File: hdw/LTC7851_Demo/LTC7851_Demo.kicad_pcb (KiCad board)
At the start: 4 copper layers, 220 parts, among them J1101 FG_LOAD, J1102 ISNS, J1103 ISNS, J1201 ISNS, J1202 ISNS, J1301 ISNS, J1302 ISNS, J1401 VOUT, J1402 LOOP_TAP, J1403 Wave_Gen_In, J201 +12VIN, J202 +12VIN, J203 +12VIN, J204 GNDIN, J205 GNDIN, J206 GNDIN, J301 CLKOUT, J302 RUN, J303 SMOD, J304 IAVG, J901 +5V OUT, J902 +5V OUT, J903 GND OUT, J904 GND OUT, Q1101 BSC123N10LSGATMA1, Q1102 BSC123N10LSGATMA1, Q1201 BSC123N10LSGATMA1, Q1202 BSC123N10LSGATMA1, Q1301 BSC123N10LSGATMA1, Q1302 BSC123N10LSGATMA1, Q201 BSC123N10LSGATMA1, Q202 BSC123N10LSGATMA1, T1401 1:1 Pulse Transformer, U1101 LT1010DD, U201 LTC4365DDB, U202 74LVC1G06, U301 LTC7851UHH, U302 74LVC1G17, U303 74LVC1G06, U304 74LVC1G06, U401 SiC779, U501 SiC779, U601 SiC779, U701 SiC779, U801 LM1117-ADJ

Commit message: Board outline, mounting holes placed
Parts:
- C1103: moved to B.Cu
- moved MH1001 240.1 mm to (3.00, -47.0)
- moved MH1003 229.4 mm to (97.0, -47.0)
- moved MH1002 223.2 mm to (50.0, -47.0)
- moved MH1004 190.3 mm to (3.00, -3.00)
- moved MH1005 184.6 mm to (50.0, -3.00)
- moved MH1006 180.3 mm to (97.0, -3.00)
- moved J1302 140.4 mm to (166.9, 177.4), turned to 270 degrees
- moved R1103 138.5 mm to (168.1, 134.8), turned to 180 degrees
- moved J1301 138.4 mm to (166.9, 164.7), turned to 270 degrees
- moved R1106 138.3 mm to (168.1, 120.5), turned to 180 degrees
- moved J1103 138.2 mm to (166.9, 113.9), turned to 270 degrees
- moved R1104 137.6 mm to (168.1, 122.1), turned to 180 degrees
- moved R1306 131.7 mm to (165.7, 181.2), turned to 180 degrees
- moved J1202 131.3 mm to (166.9, 152.0), turned to 270 degrees
- moved R1105 129.9 mm to (168.1, 133.2), turned to 180 degrees
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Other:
- board outline added: 100 x 50 mm
- board text added: "Active Load"
- board text added: "Load Gate Driver"

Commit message: Arranged components for phase 1
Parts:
- moved C401 200.5 mm to (235.0, 94.4)
- moved C403 200.5 mm to (235.0, 93.1)
- moved C404 200.5 mm to (250.2, 83.2)
- moved C406 200.5 mm to (250.1, 85.4)
- moved R402 200.5 mm to (244.2, 92.3)
- moved R404 200.5 mm to (250.0, 86.8)
- moved R409 200.5 mm to (243.4, 93.7)
- moved R410 200.5 mm to (250.0, 88.3)
- moved C402 200.5 mm to (237.8, 92.9)
- moved R401 200.5 mm to (247.1, 89.4)
- moved R403 200.5 mm to (252.9, 83.3)
- moved R408 200.5 mm to (252.8, 86.2)
- moved R411 200.5 mm to (246.8, 92.4)
- moved C408 82.4 mm to (-32.4, 42.3)
- moved C418 77.3 mm to (-24.8, 68.1), turned to 270 degrees
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
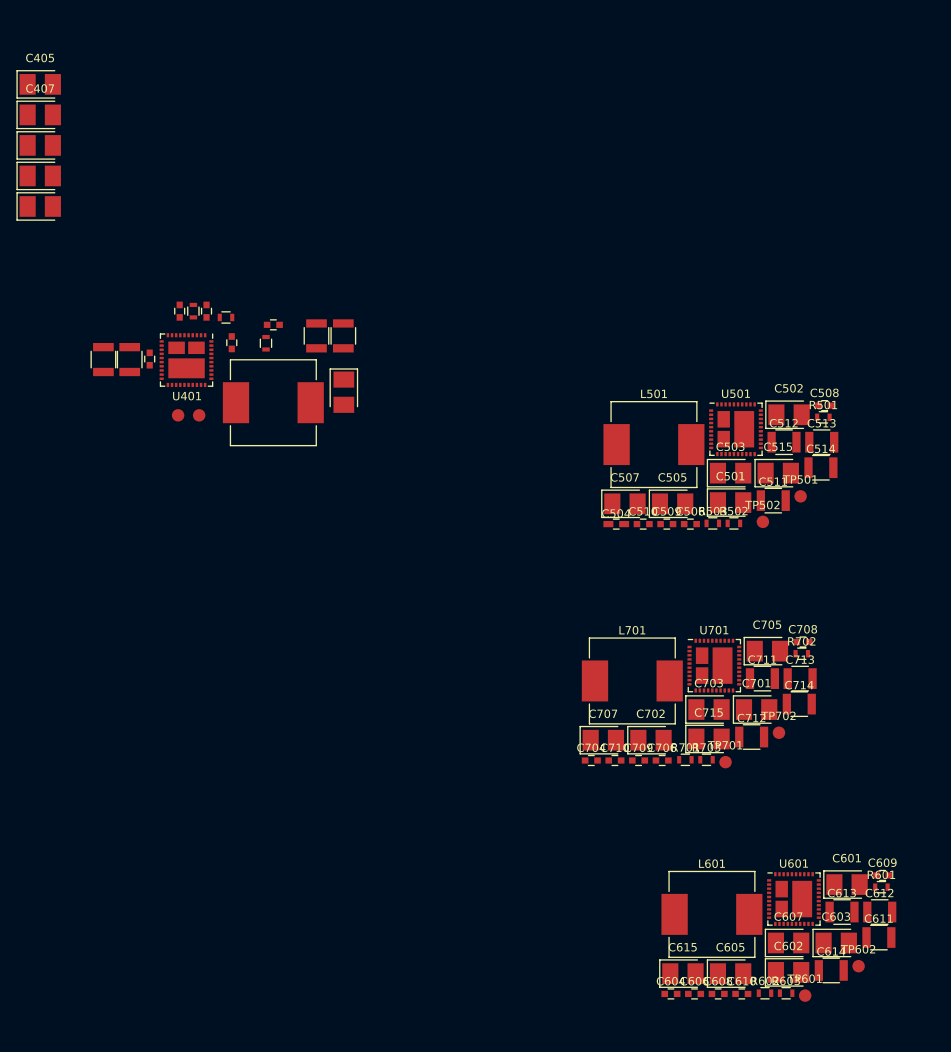
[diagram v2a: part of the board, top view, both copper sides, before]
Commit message: Duplicated phase 1 four times and changed ref des
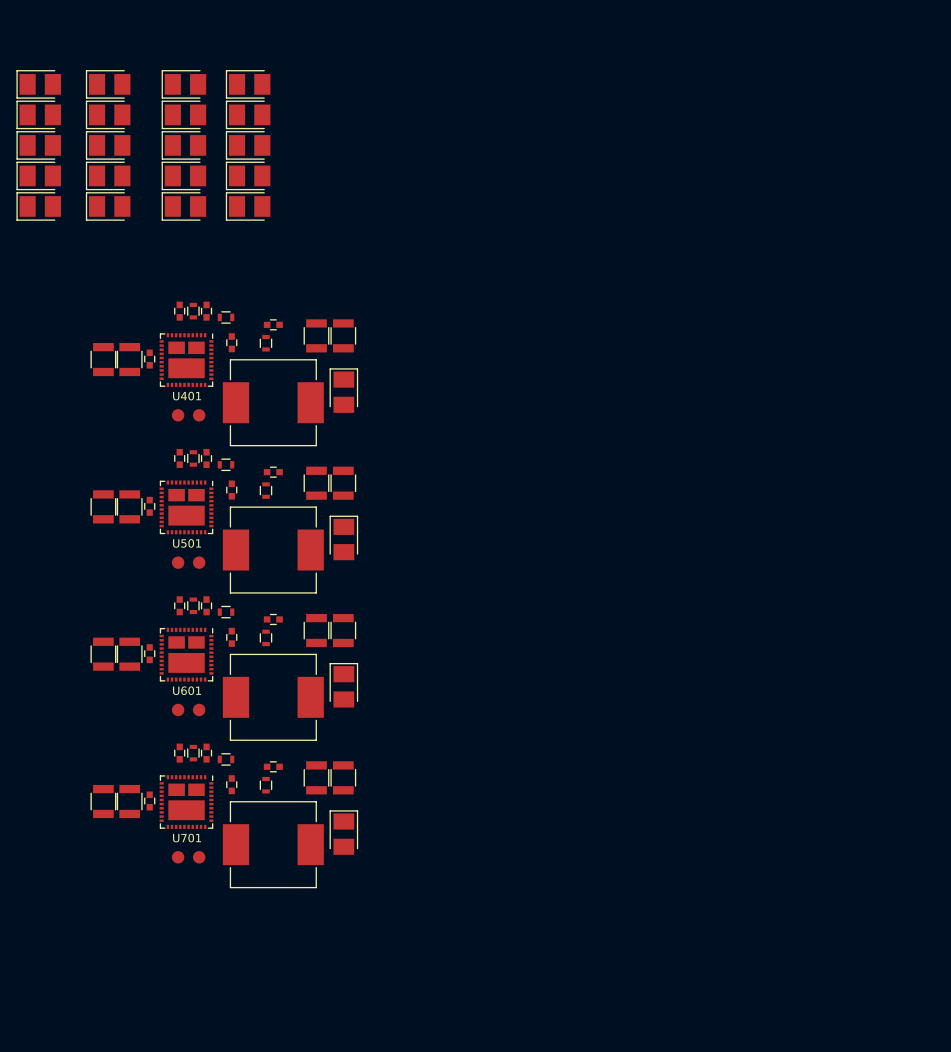
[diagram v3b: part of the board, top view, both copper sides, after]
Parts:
- C504: footprint Capacitors_SMD:C_0603_HandSoldering -> Capacitors_SMD:C_0603
- moved C602 126.5 mm to (-14.9, 38.6)
- moved C601 125.3 mm to (-14.9, 34.9)
- moved C603 124.2 mm to (-14.9, 42.3)
- moved C605 116.6 mm to (-14.9, 46.0)
- moved C607 114.9 mm to (-14.9, 49.7)
- moved C701 97.1 mm to (-7.11, 34.9)
- moved C611 96.7 mm to (-21.6, 103.7), turned to 270 degrees
- moved C613 94.4 mm to (-24.8, 103.7), turned to 270 degrees
- moved C609 92.4 mm to (-19.2, 103.6), turned to 270 degrees
- moved C501 90.3 mm to (-24.0, 34.9)
- moved C702 89.7 mm to (-7.11, 38.6)
- moved C502 89.6 mm to (-24.0, 38.6)
- moved C703 87.8 mm to (-7.11, 42.3)
- moved C513 87.0 mm to (-24.8, 85.9), turned to 270 degrees
- moved R601 85.8 mm to (-9.97, 98.6)
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
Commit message: Placed phases on board
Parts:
- removed J1103, J1201, J1202, J1301, J1302: ISNS, Pin_Headers:Pin_Header_Straight_1x02_Pitch2.54mm
- J1102, Q1101, Q1102, Q1201, Q1202, Q1301, Q1302, R1103, R1104, R1105, R1106, R1107, R1108, R1201, R1202, R1203, R1204, R1205, R1206, R1301, R1302, R1303, R1304, R1305, R1306: moved to B.Cu
- moved J904 202.2 mm to (23.4, -4.95)
- moved J901 198.8 mm to (40.3, -4.95)
- moved J903 183.0 mm to (66.0, -4.95)
- moved J902 178.2 mm to (82.9, -4.95)
- moved C713 175.4 mm to (40.2, -41.4), turned to 180 degrees
- moved C711 171.2 mm to (40.2, -38.2), turned to 180 degrees
- moved C709 168.1 mm to (40.3, -35.8), turned to 180 degrees
- moved TP701 168.0 mm to (33.5, -32.4), turned to 270 degrees
- moved C613 166.8 mm to (57.5, -41.4), turned to 180 degrees
- moved TP702 164.8 mm to (33.5, -29.8), turned to 270 degrees
- moved C611 162.5 mm to (57.5, -38.2), turned to 180 degrees
- moved U701 162.5 mm to (40.1, -31.4), turned to 180 degrees
- moved C513 161.6 mm to (74.7, -41.4), turned to 180 degrees
- moved C708 160.1 mm to (46.0, -32.2), turned to 180 degrees
- moved C418 160.1 mm to (92.0, -41.4), turned to 180 degrees
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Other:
- board text added: "-VOUT+"

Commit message: Finished arranging parts on board
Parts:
- removed J202, J203: +12VIN, Custom Footprints Library:Keystone_8191
- removed J204, J205: GNDIN, Custom Footprints Library:Keystone_8191
- C1101, C1102, C302, C303, C405, C407, C408, C410, C412, C501, C502, C503, C505, C507, C601, C602, C603, C605, C701, R1101, R1102, R302, R310, U1101: moved to B.Cu
- J1102: moved to F.Cu
- J201: value +12VIN -> +12V IN; footprint Custom Footprints Library:Keystone_8191 -> Custom Footprints Library:Wuerth_7461096_M4_Shank_9pos
- J206: value GNDIN -> GND IN; footprint Custom Footprints Library:Keystone_8191 -> Custom Footprints Library:Wuerth_7461096_M4_Shank_9pos
- TP201: footprint Pin_Headers:Pin_Header_Angled_1x01_Pitch2.54mm -> Pin_Headers:Pin_Header_Straight_1x01_Pitch2.54mm
- moved C603 196.8 mm to (171.8, 104.6), turned to 90 degrees
- moved C601 192.3 mm to (164.4, 104.6), turned to 90 degrees
- moved C605 192.1 mm to (168.1, 104.6), turned to 90 degrees
- moved C701 189.7 mm to (166.4, 111.7), turned to 270 degrees
- moved C505 189.4 mm to (153.6, 111.6), turned to 270 degrees
- moved C507 189.2 mm to (157.1, 104.6), turned to 90 degrees
- moved C602 187.6 mm to (160.7, 104.6), turned to 90 degrees
- moved C503 187.2 mm to (149.9, 111.6), turned to 270 degrees
- moved C702 176.5 mm to (151.9, 115.1), turned to 180 degrees
- moved C502 176.3 mm to (136.6, 111.4), turned to 270 degrees
- moved C501 174.6 mm to (132.9, 111.4), turned to 270 degrees
- moved C412 164.1 mm to (122.3, 104.5), turned to 90 degrees
- moved J1403 163.7 mm to (90.3, 113.4), turned to 90 degrees
- moved C407 161.1 mm to (111.3, 111.5), turned to 270 degrees
- moved C405 159.6 mm to (107.7, 111.5), turned to 270 degrees
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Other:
- board text removed: "+5.5 MNG"
- board text removed: "Active Load"
- board text removed: "Load Gate Driver"

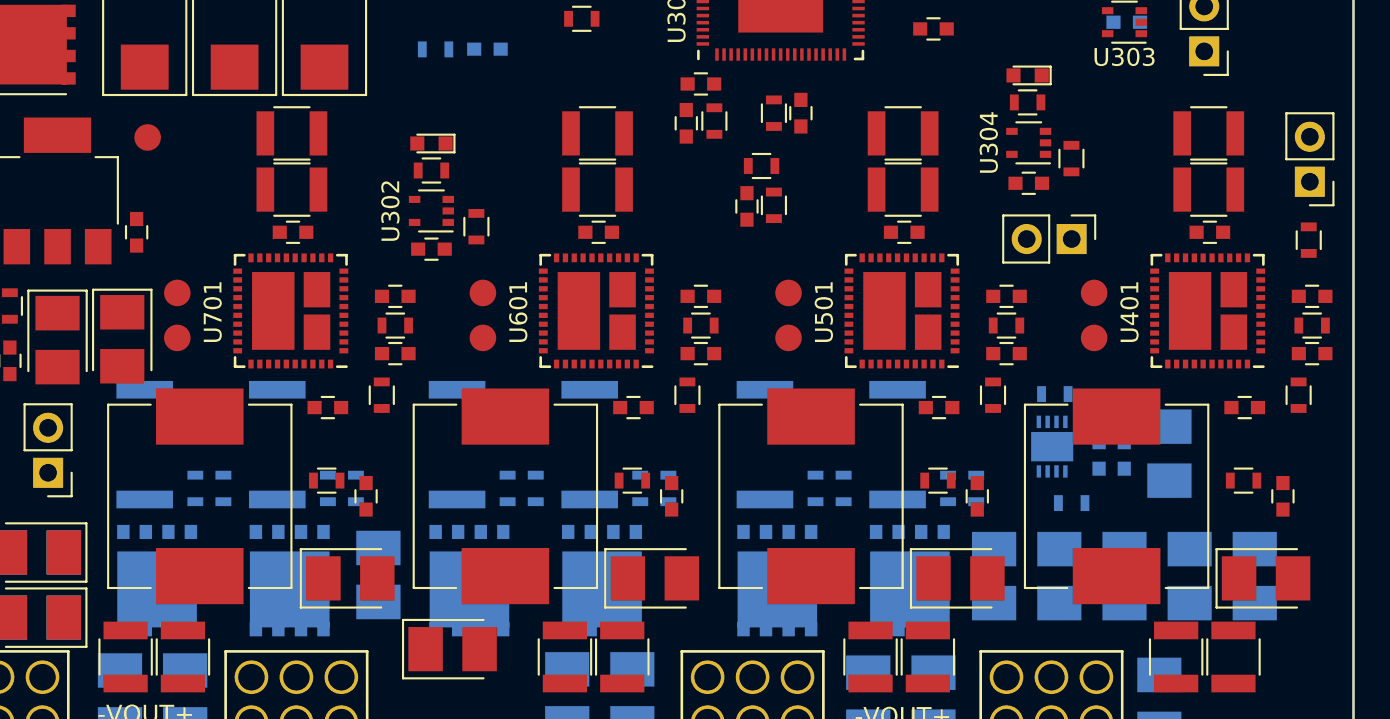
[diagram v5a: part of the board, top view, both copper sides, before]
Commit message: Flipped order of phases on PCB
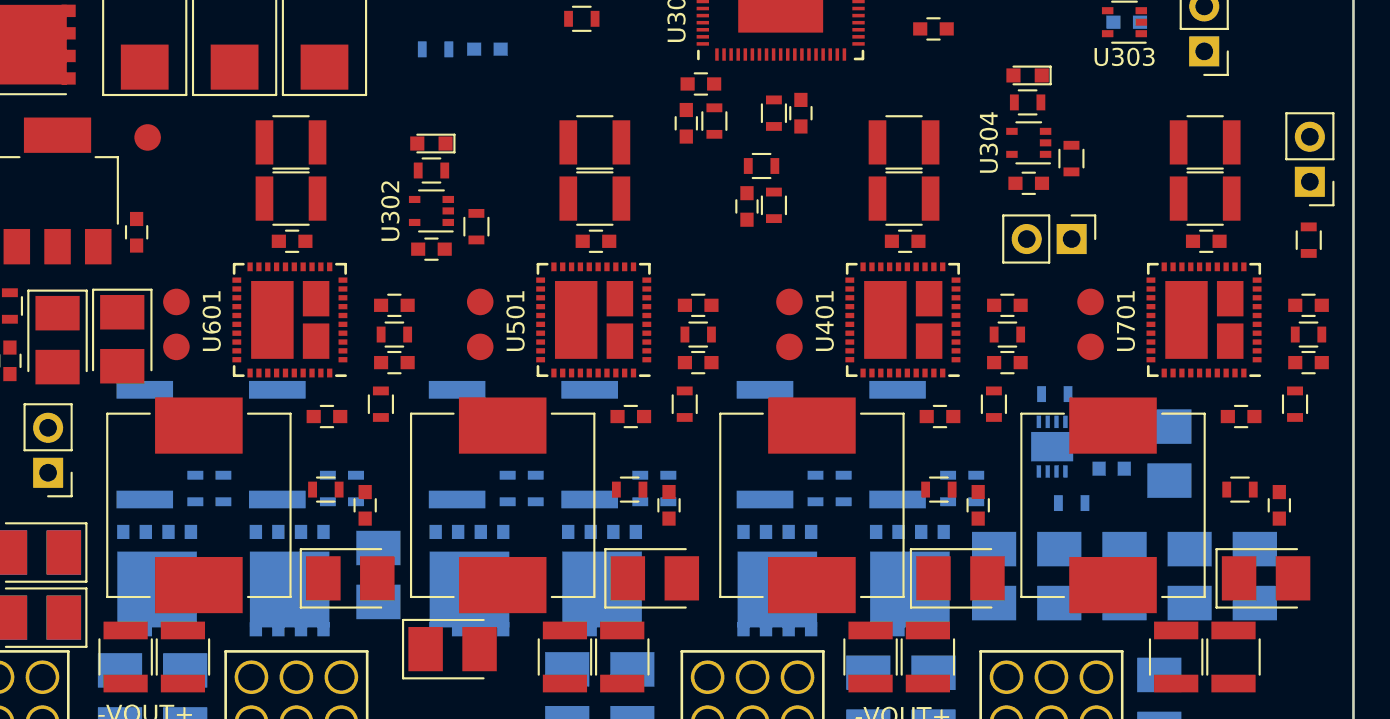
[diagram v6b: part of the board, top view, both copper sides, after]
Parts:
- moved C704 51.6 mm to (174.8, 92.5)
- moved C706 51.6 mm to (171.0, 95.6)
- moved C708 51.6 mm to (174.8, 89.3)
- moved C709 51.6 mm to (169.0, 85.7)
- moved L701 51.6 mm to (163.8, 100.6)
- moved R701 51.6 mm to (174.1, 94.9)
- moved R702 51.6 mm to (174.8, 90.9)
- moved R703 51.6 mm to (171.0, 99.7)
- moved C710 51.6 mm to (173.2, 100.6)
- moved C711 51.6 mm to (169.0, 83.3)
- moved C713 51.6 mm to (169.0, 80.1)
- moved TP701 51.6 mm to (162.5, 89.1)
- moved TP702 51.6 mm to (162.5, 91.6)
- moved U701 51.6 mm to (168.9, 90.1)
- moved TP501 17.4 mm to (128.0, 89.1)
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
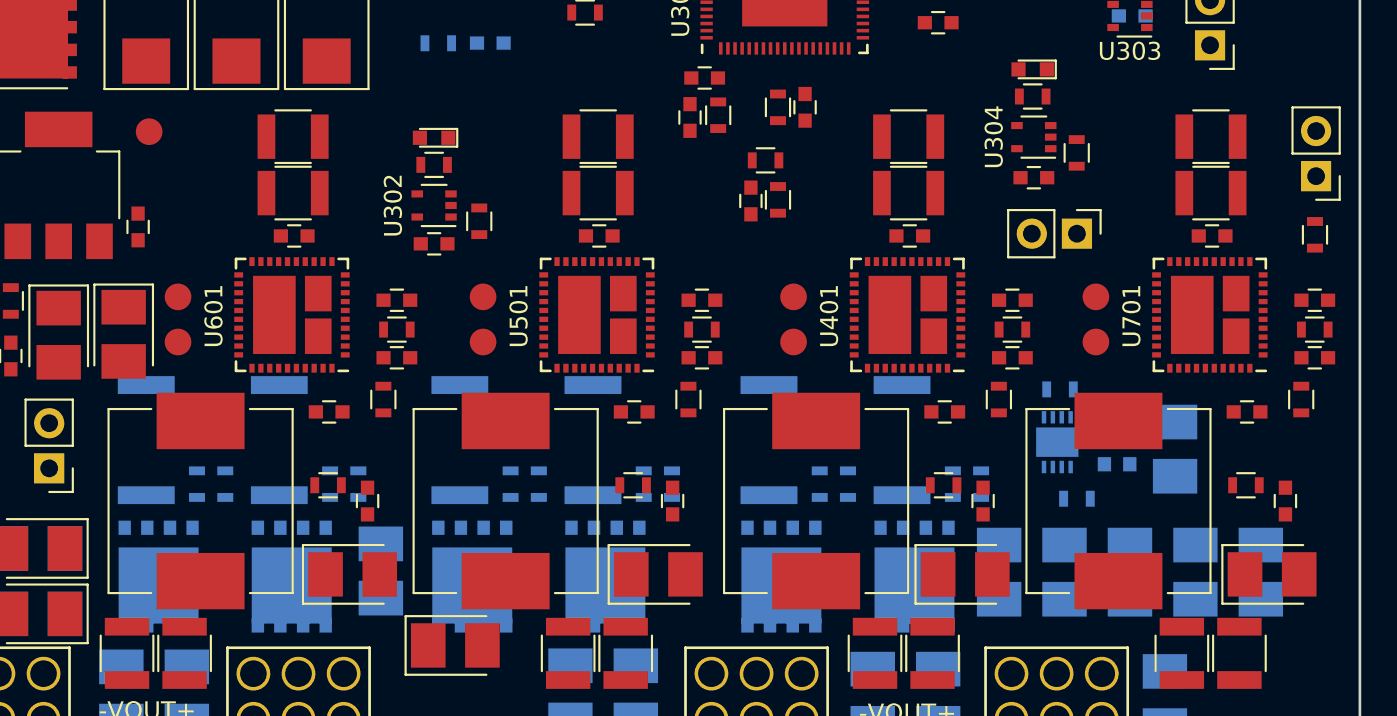
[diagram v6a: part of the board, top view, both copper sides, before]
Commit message: Flipped phases again, better order now
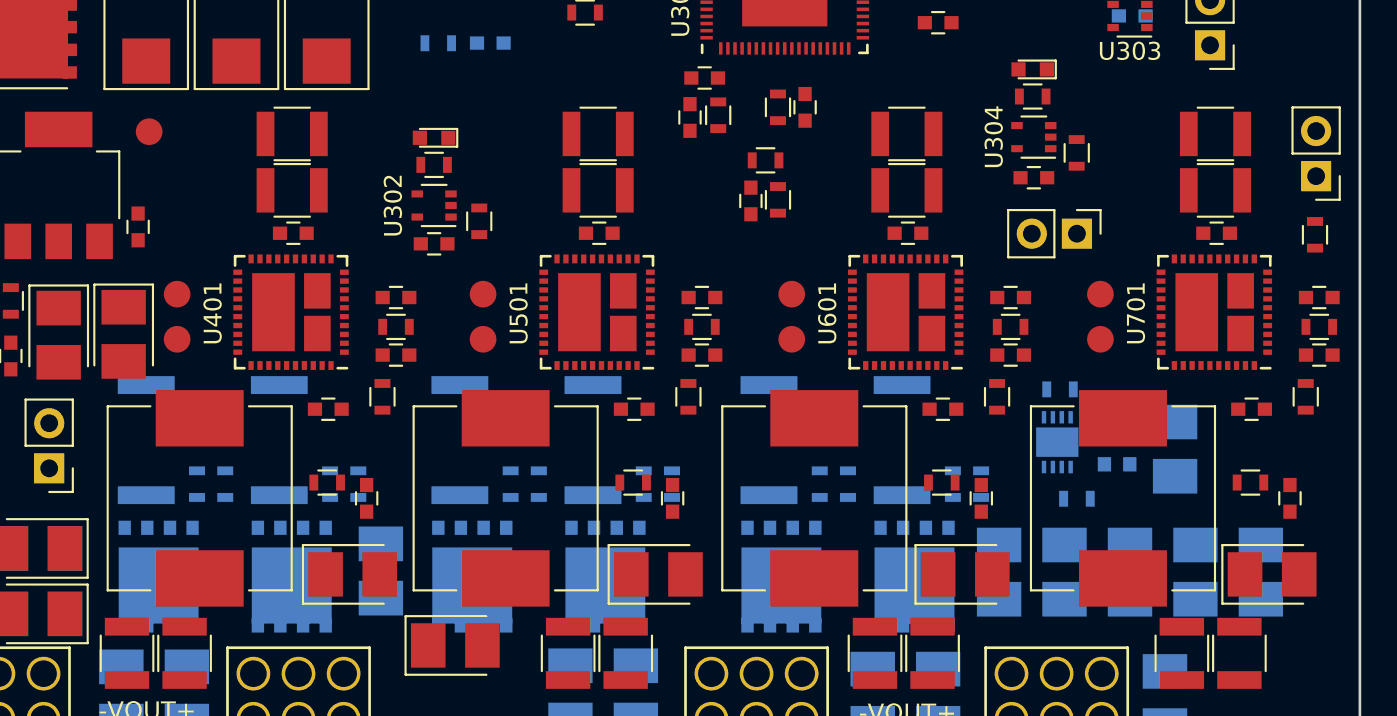
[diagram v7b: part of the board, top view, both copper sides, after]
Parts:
- moved C409 34.7 mm to (123.1, 92.4)
- moved C411 34.7 mm to (119.3, 95.4)
- moved C413 34.7 mm to (123.1, 89.1)
- moved R405 34.7 mm to (122.4, 94.7)
- moved R406 34.7 mm to (123.1, 90.8)
- moved C414 34.7 mm to (117.3, 85.5)
- moved C415 34.7 mm to (121.5, 100.4)
- moved C416 34.7 mm to (117.3, 83.1)
- moved C418 34.7 mm to (117.3, 79.9)
- moved L401 34.7 mm to (112.1, 100.4)
- moved R407 34.7 mm to (119.2, 99.6)
- moved TP401 34.7 mm to (110.8, 89.0)
- moved TP402 34.7 mm to (110.8, 91.5)
- moved U401 34.7 mm to (117.2, 90.0)
- moved C609 34.5 mm to (151.9, 85.5)
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
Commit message: Added GND plane
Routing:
- added copper zone on GND, net GND
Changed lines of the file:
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@@
   (gr_line (start 177.3684 117.2972) (end 177.3684 67.2972) (layer Edge.Cuts) (width 0.15))
   (gr_line (start 77.3684 117.2972) (end 177.3684 117.2972) (layer Edge.Cuts) (width 0.15))
+  (zone (net 2) (net_name GND) (layer GND) (hatch edge 0.508)
+    (connect_pads yes (clearance 0.254))
+    (min_thickness 0.254)
+    (fill yes (arc_segments 16) (thermal_gap 0.508) (thermal_bridge_width 0.508) (smoothing fillet) (radius 0.635))
+    (polygon
+      (pts
+        (xy 77.3684 67.31) (xy 136.5504 67.5132) (xy 177.3428 67.31) (xy 177.3428 117.2972) (xy 77.3684 117.2972)
+      )
+    )
+  )
 )
